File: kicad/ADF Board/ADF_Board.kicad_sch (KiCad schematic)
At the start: 3 parts, among them J1 Conn_Coaxial, J14 Conn_Coaxial, J3 Conn_Coaxial

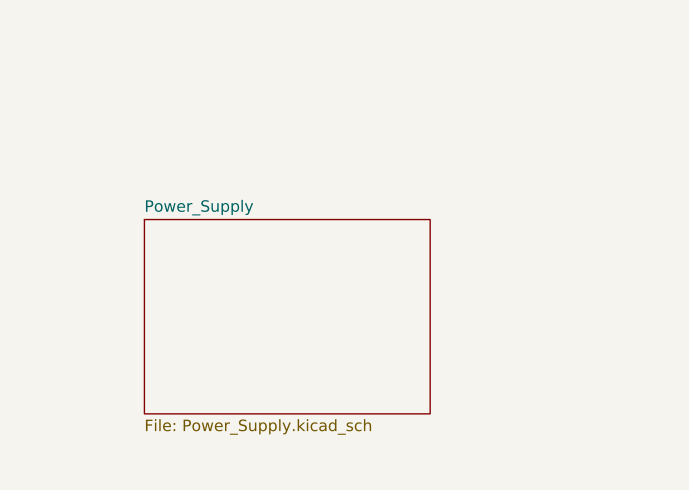
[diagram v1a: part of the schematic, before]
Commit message: added screw holes
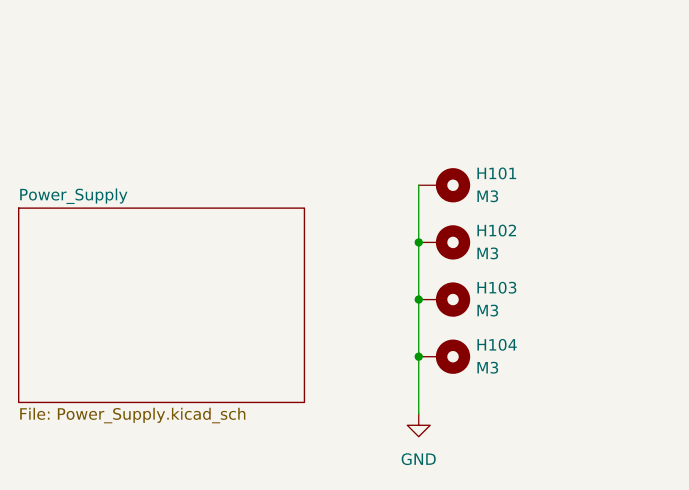
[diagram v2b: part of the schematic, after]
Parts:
- added H101: M3, MountingHole:MountingHole_3.2mm_M3_Pad_Via, symbol Mechanical:MountingHole_Pad
- added H102, H103, H104: M3, symbol Mechanical:MountingHole_Pad
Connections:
- net GND: now also H101.1, H102.1, H103.1, H104.1

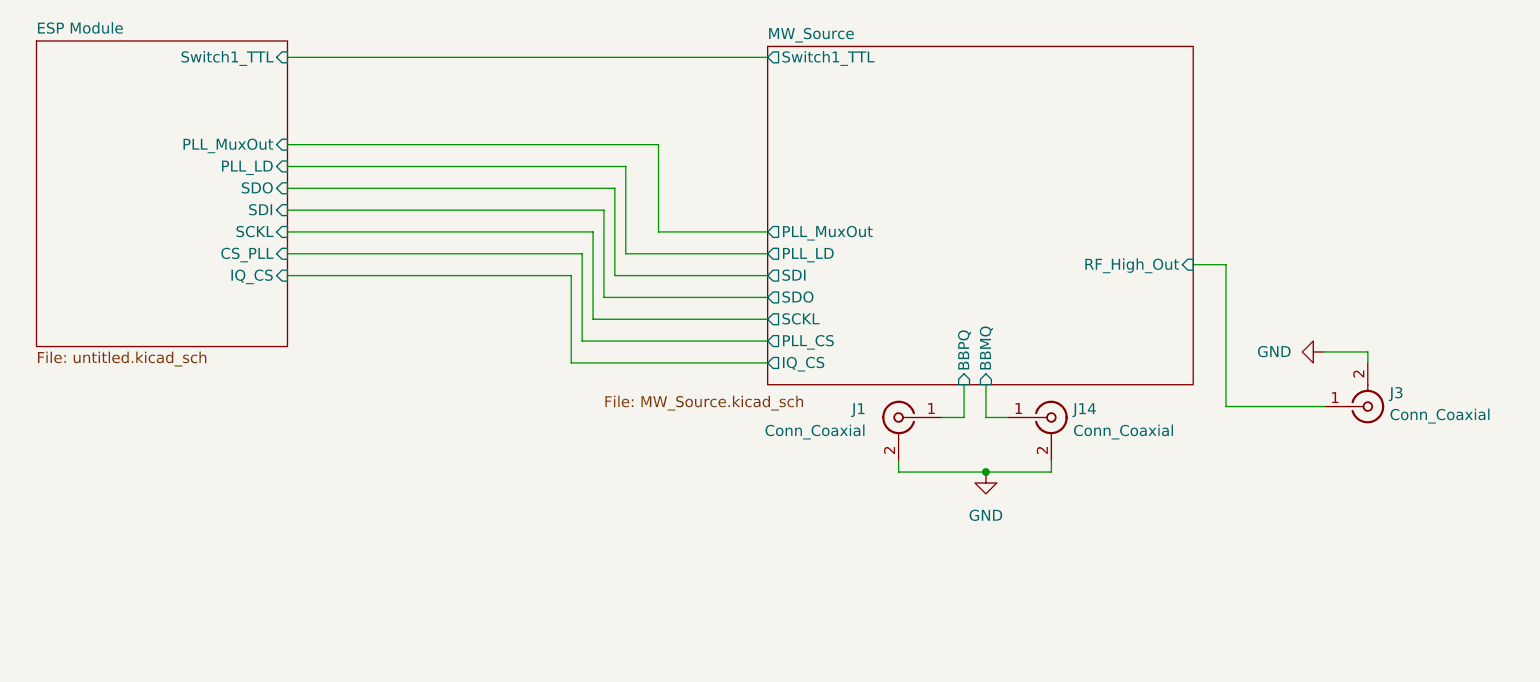
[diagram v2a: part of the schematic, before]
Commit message: Deleted I/Q mod, switch, charge pump Found candidates for RF amp and PLL
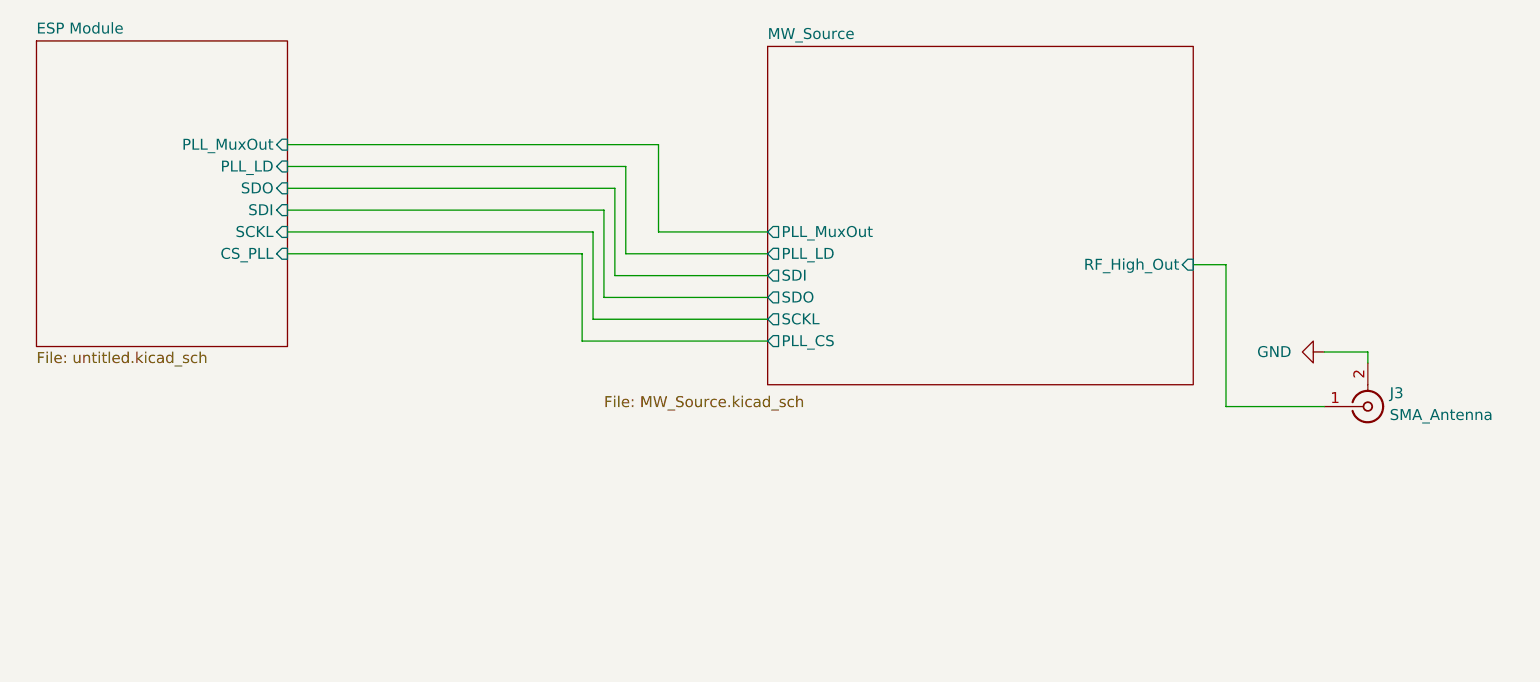
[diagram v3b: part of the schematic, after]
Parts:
- removed J1, J14: Conn_Coaxial, Connector_Coaxial:U.FL_Hirose_U.FL-R-SMT-1_Vertical, symbol Connector:Conn_Coaxial
- J3: value Conn_Coaxial -> SMA_Antenna
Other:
- sheet ESP Module ports: added none; removed IQ_CS, Switch1_TTL
- sheet MW_Source ports: added none; removed BBMQ, BBPQ, IQ_CS, Switch1_TTL

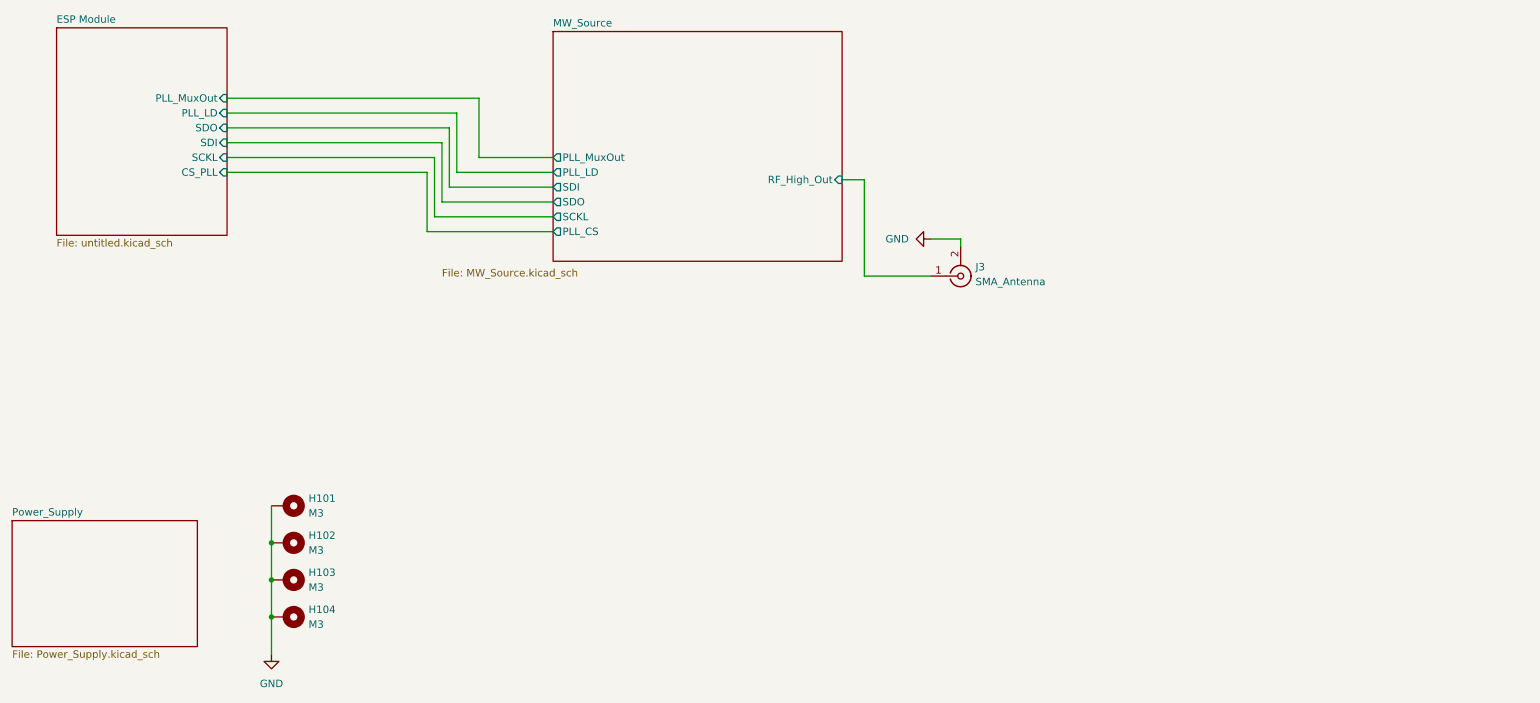
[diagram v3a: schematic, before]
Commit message: Finished part selection and rearranged schematic
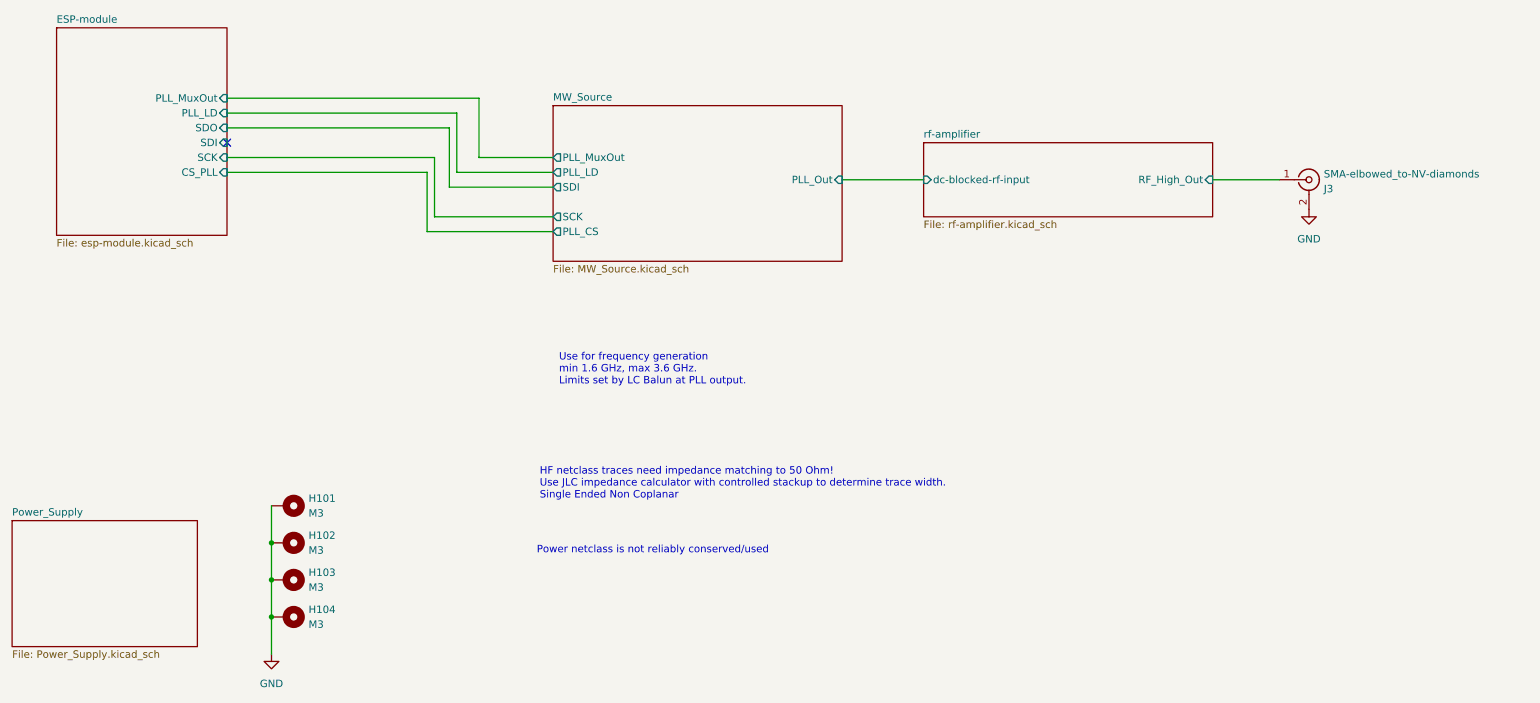
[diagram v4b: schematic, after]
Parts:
- H102, H103, H104: footprint (none) -> MountingHole:MountingHole_3.2mm_M3_Pad_Via
- J3: value SMA_Antenna -> SMA-elbowed_to-NV-diamonds; footprint Connector_Coaxial:SMA_Amphenol_132289_EdgeMount -> Connector_Coaxial:SMA_BAT_Wireless_BWSMA-KWE-Z001; LCSC (none) -> C496551
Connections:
- net MW_Source/RF_High_Out renamed rf-amplifier/RF_High_Out
- no-connect marks 0 -> 1
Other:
- sheet ESP Module renamed ESP-module
- added sheet rf-amplifier (rf-amplifier.kicad_sch)
- sheet ESP-module: file untitled.kicad_sch -> esp-module.kicad_sch
- sheet ESP-module ports: added SCK; removed SCKL
- sheet MW_Source ports: added PLL_Out, SCK; removed RF_High_Out, SCKL, SDO
- note added: "HF netclass traces need impedance matching to 50 Ohm! Use JLC impedance calculator with controlled stackup to determine trace width. Single Ended Non Coplanar"
- note added: "Power netclass is not reliably conserved/used"
- note added: "Use for frequency generation min 1.6 GHz, max 3.6 GHz. Limits set by LC Balun at PLL output."
- moved on the sheet: J3
